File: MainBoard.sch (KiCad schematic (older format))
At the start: 34 parts, among them J1 CONN_1x4, J2 CONN_2X3, J3 CONN_2X3, J5 SWDEBUG_CONNECTOR, J7 CONN_2X12, J8 CONN_1X2, U1 VX07805-1000, U2 TPS2115A, U3 ld1117s33

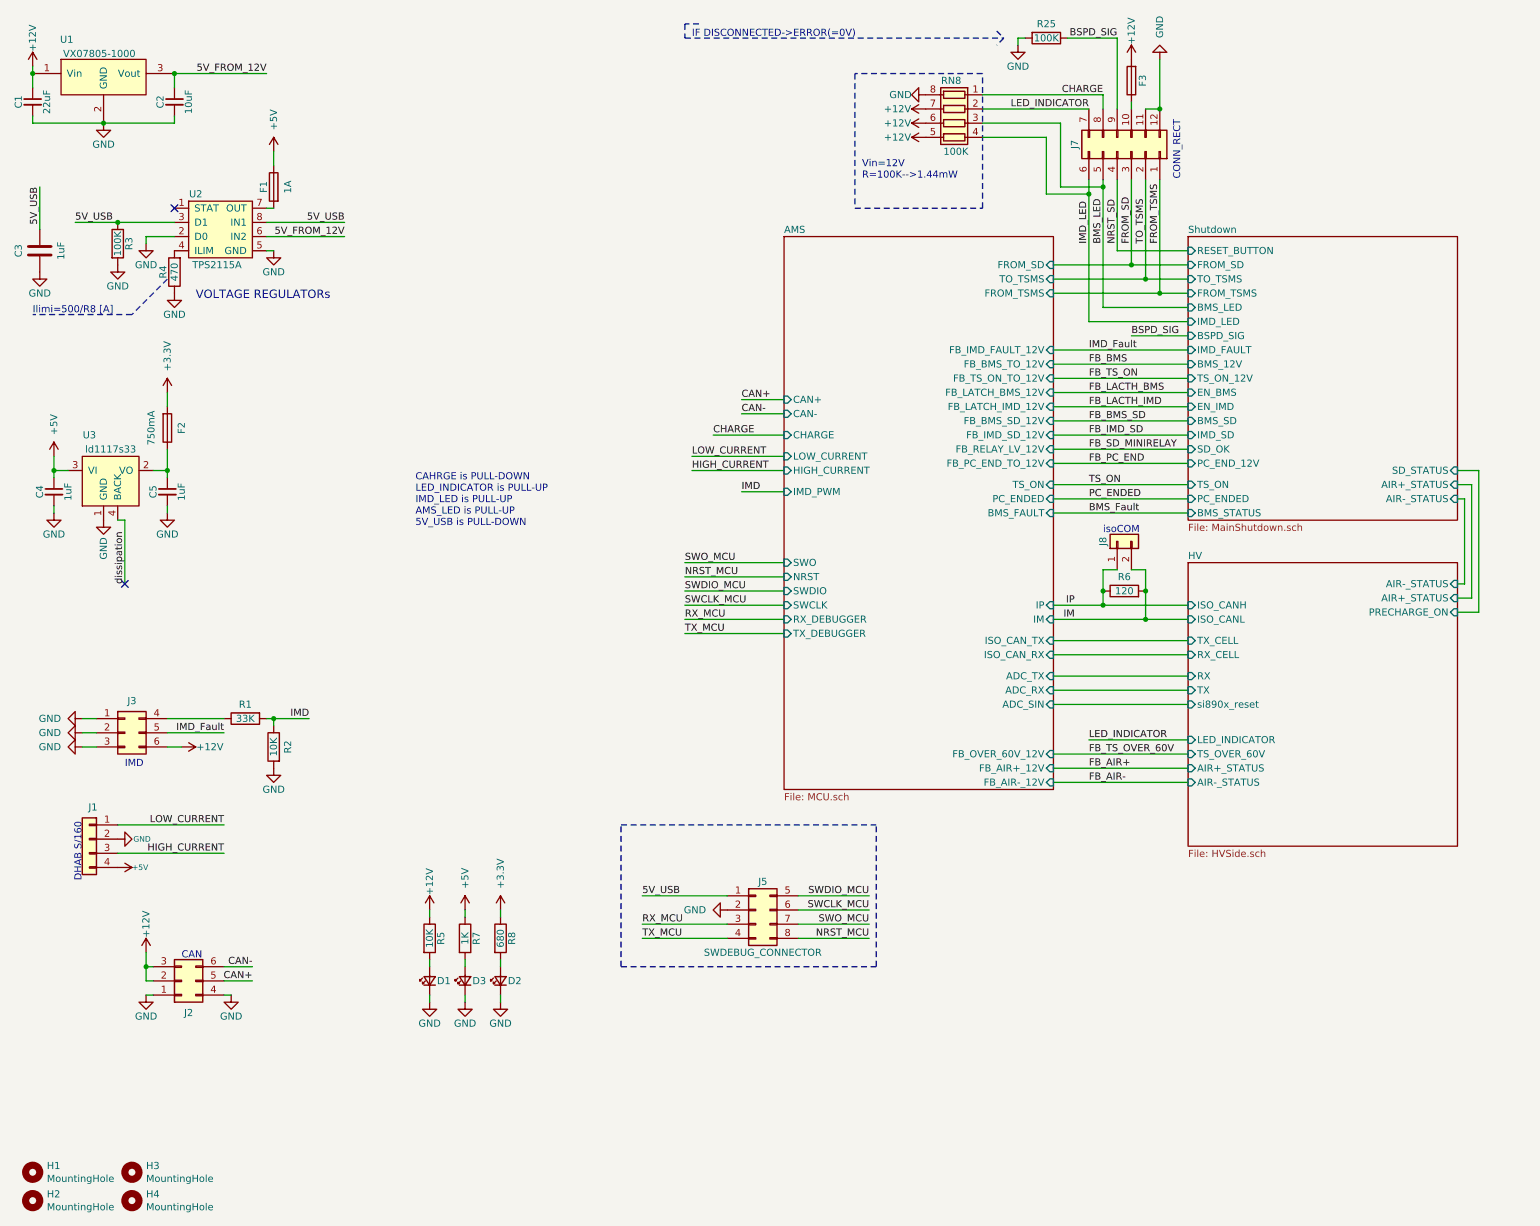
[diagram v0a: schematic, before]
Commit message: added a lot of annotations and readability in the schematic, not complete
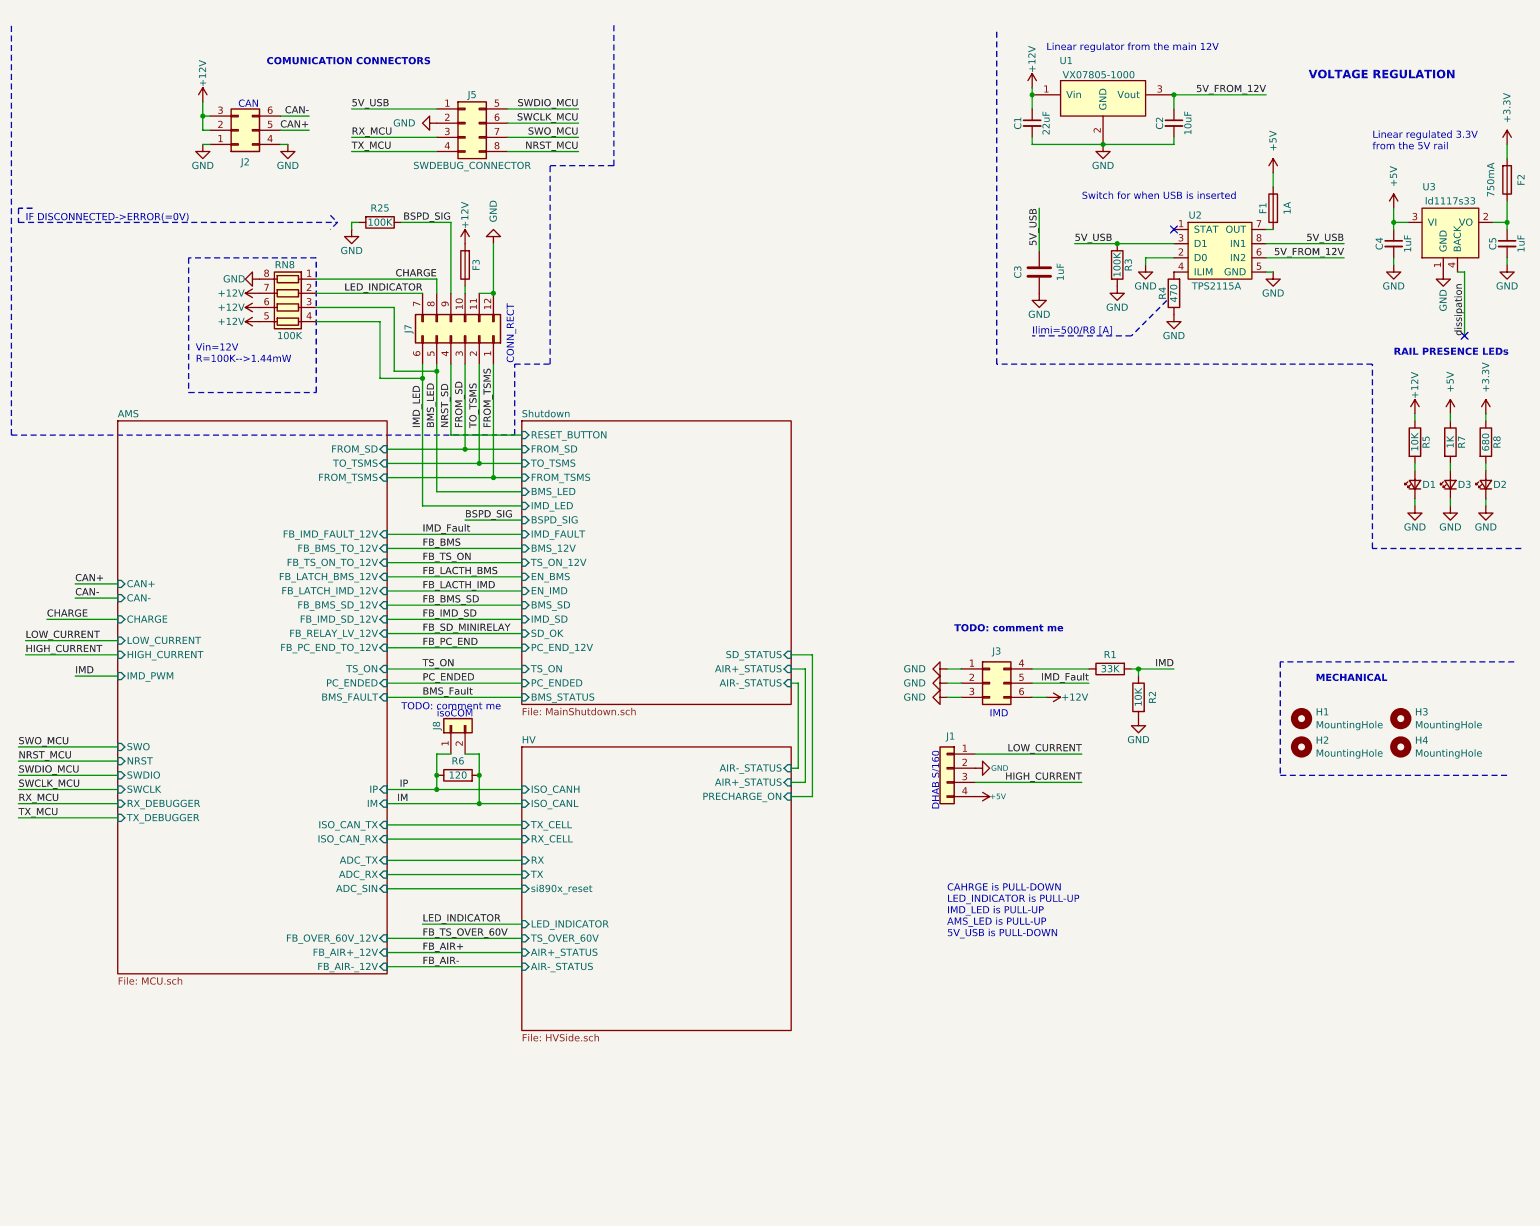
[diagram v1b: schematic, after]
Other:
- note added: "COMUNICATION CONNECTORS"
- note added: "Linear regulated 3.3V \nfrom the 5V rail"
- note added: "Linear regulator from the main 12V"
- note added: "MECHANICAL"
- note added: "RAIL PRESENCE LEDs"
- note added: "Switch for when USB is inserted"
- note added: "TODO: comment me"
- note added: "VOLTAGE REGULATION"
- note removed: "VOLTAGE REGULATORs"
- moved on the sheet: C1, C2, C3, C4, C5, D1, D2, D3, F1, F2, F3, H1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
